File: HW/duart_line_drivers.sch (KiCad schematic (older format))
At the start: 2 parts

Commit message: Added ram, vias, rtc and ide connector. Managed to delete Pluto's CPLD schemas.
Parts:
- removed U?: SC26C92, symbol SC26C92
- removed U?: MAX238, symbol MAX238
- added C1, C2, C3, C4, C5: 1.0uF, symbol CP_Small
- added C6: 0.1uF, symbol C
- added J1: RS232a, symbol Conn_02x05_Odd_Even
- added J2: RS232b, symbol Conn_02x05_Odd_Even
- added U3: MAX238, symbol MAX238-RESCUE-saturn
- added U4: SC28L92PLCC44, symbol SC28L92PLCC44
- added X1: 3.6864 MHz, Oscillators:Oscillator_DIP-8, symbol CXO_DIP8
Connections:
- net labels added: A[0..18], A[0..3], CTSa, CTSb, D0, D1, D2, D3, D4, D5, D6, D7, D[0..7], GND, RES, RS232CTSa, RS232CTSb, RS232RTSa, RS232RTSb, RS232RxDa, RS232RxDb, RS232TxDa, RS232TxDb, RTSa, RTSb, VCC, ~IRQ, ~MRD, ~MWR
- wire segments 0 -> 96
- no-connect marks 0 -> 23

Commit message: Address, databus and control signals added to RAM and ROM
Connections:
- net ~DUARTSEL: now reaches U4.39 (~CEN)
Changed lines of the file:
@@
 Sheet 3 6
 Title "Saturn SBC"
-Date "2017-06-28"
-Rev "1.0"
+Date "2017-12-23"
+Rev "0.1"
 Comp "Linux Grotto"
 Comment1 ""
@@
 Wire Wire Line
 	2100 3650 2025 3650
+Text HLabel 7800 3625 2    60   Input ~ 0
+~DUARTSEL
+Wire Wire Line
+	7400 3625 7800 3625
 $EndSCHEMATC

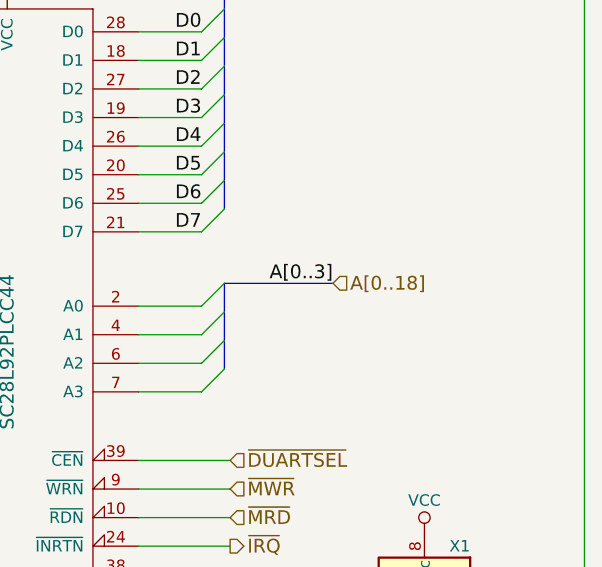
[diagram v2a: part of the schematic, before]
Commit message: Simulation of address decoding.
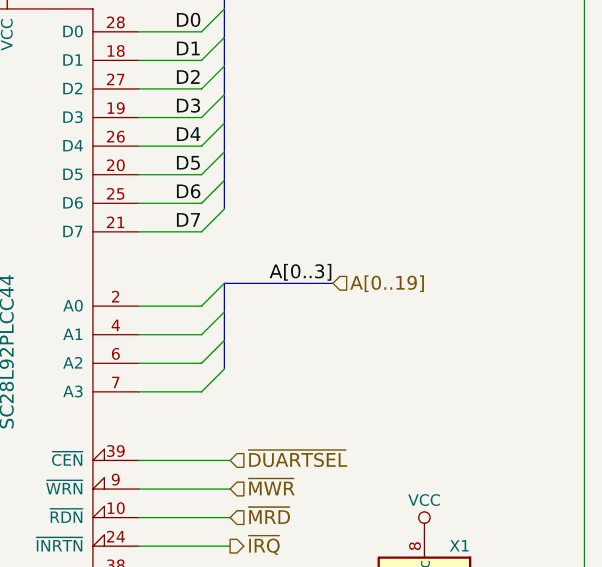
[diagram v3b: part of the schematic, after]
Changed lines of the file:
@@
 A[0..3]
 Text HLabel 8250 2850 2    60   Input ~ 0
-A[0..18]
+A[0..19]
 $Comp
 L MAX238-RESCUE-saturn U3
@@
 $EndComp
 $Comp
-L VCC #PWR5
+L VCC #PWR6
 U 1 1 5A14EA51
 P 4025 1225
-F 0 "#PWR5" H 4025 1075 50  0001 C CNN
+F 0 "#PWR6" H 4025 1075 50  0001 C CNN
 F 1 "VCC" H 4025 1375 50  0000 C CNN
 F 2 "" H 4025 1225 50  0001 C CNN
@@
 $EndComp
 $Comp
-L GND #PWR7
+L GND #PWR8
 U 1 1 5A14EB59
 P 5075 1350
-F 0 "#PWR7" H 5075 1100 50  0001 C CNN
+F 0 "#PWR8" H 5075 1100 50  0001 C CNN
 F 1 "GND" V 5075 1150 50  0000 C CNN
 F 2 "" H 5075 1350 50  0001 C CNN
@@
 $EndComp
 $Comp
-L GND #PWR4
+L GND #PWR5
 U 1 1 5A14F46D
 P 3125 2225
-F 0 "#PWR4" H 3125 1975 50  0001 C CNN
+F 0 "#PWR5" H 3125 1975 50  0001 C CNN
 F 1 "GND" H 3125 2075 50  0000 C CNN
 F 2 "" H 3125 2225 50  0001 C CNN
@@
 $EndComp
 $Comp
-L GND #PWR6
+L GND #PWR7
 U 1 1 5A14F656
 P 4025 4450
-F 0 "#PWR6" H 4025 4200 50  0001 C CNN
+F 0 "#PWR7" H 4025 4200 50  0001 C CNN
 F 1 "GND" H 4025 4300 50  0000 C CNN
 F 2 "" H 4025 4450 50  0001 C CNN
@@
 	1150 3550 1150 3725
 $Comp
-L GND #PWR3
+L GND #PWR4
 U 1 1 5A1536E4
 P 1150 3725
-F 0 "#PWR3" H 1150 3475 50  0001 C CNN
+F 0 "#PWR4" H 1150 3475 50  0001 C CNN
 F 1 "GND" H 1150 3575 50  0000 C CNN
 F 2 "" H 1150 3725 50  0001 C CNN
@@
 	1150 2825 1150 3000
 $Comp
-L GND #PWR2
+L GND #PWR3
 U 1 1 5A153732
 P 1150 3000
-F 0 "#PWR2" H 1150 2750 50  0001 C CNN
+F 0 "#PWR3" H 1150 2750 50  0001 C CNN
 F 1 "GND" H 1150 2850 50  0000 C CNN
 F 2 "" H 1150 3000 50  0001 C CNN
@@
 $EndComp
 $Comp
-L VCC #PWR10
+L VCC #PWR11
 U 1 1 5A1570C4
 P 8650 3950
-F 0 "#PWR10" H 8650 3800 50  0001 C CNN
+F 0 "#PWR11" H 8650 3800 50  0001 C CNN
 F 1 "VCC" H 8650 4100 50  0000 C CNN
 F 2 "" H 8650 3950 50  0001 C CNN
@@
 $EndComp
 $Comp
-L GND #PWR11
+L GND #PWR12
 U 1 1 5A157100
 P 8650 4550
-F 0 "#PWR11" H 8650 4300 50  0001 C CNN
+F 0 "#PWR12" H 8650 4300 50  0001 C CNN
 F 1 "GND" H 8650 4400 50  0000 C CNN
 F 2 "" H 8650 4550 50  0001 C CNN
@@
 	7400 4500 7800 4500
 $Comp
-L VCC #PWR9
+L VCC #PWR10
 U 1 1 5A157C4F
 P 7800 4500
-F 0 "#PWR9" H 7800 4350 50  0001 C CNN
+F 0 "#PWR10" H 7800 4350 50  0001 C CNN
 F 1 "VCC" V 7800 4675 50  0000 C CNN
 F 2 "" H 7800 4500 50  0001 C CNN
@@
 	6825 4900 6825 5325
 $Comp
-L GND #PWR8
+L GND #PWR9
 U 1 1 5A157EAF
 P 6825 5325
-F 0 "#PWR8" H 6825 5075 50  0001 C CNN
+F 0 "#PWR9" H 6825 5075 50  0001 C CNN
 F 1 "GND" H 6825 5175 50  0000 C CNN
 F 2 "" H 6825 5325 50  0001 C CNN

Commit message: ABEL code passes compilation, no tests though. Small changes to schema
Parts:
- added R5: 470, Resistors_ThroughHole:R_Axial_DIN0207_L6.3mm_D2.5mm_P2.54mm_Vertical, symbol R_Small
- C1, C2, C3, C4, C5: footprint (none) -> Capacitors_ThroughHole:CP_Radial_Tantal_D4.5mm_P2.50mm
- C6: footprint (none) -> Capacitors_ThroughHole:C_Disc_D4.7mm_W2.5mm_P5.00mm
- J1, J2: footprint (none) -> Connectors_IDC:IDC-Header_2x05_Pitch2.54mm_Straight
- U3: footprint (none) -> Housings_DIP:DIP-24_W7.62mm_Socket
- U4: footprint (none) -> saturn:PLCC-44_THT-Socket
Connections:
- net VCC: now also C6.2, U4.44 (VCC), R5.1
- net A0: now reaches U4.2 (A0)
- net at U4.36 (X1/CLK), X1.5 (OUT): now also R5.2
- net A1: now reaches U4.4 (A1)
- net A2: now reaches U4.6 (A2)
- net A3: now reaches U4.7 (A3)

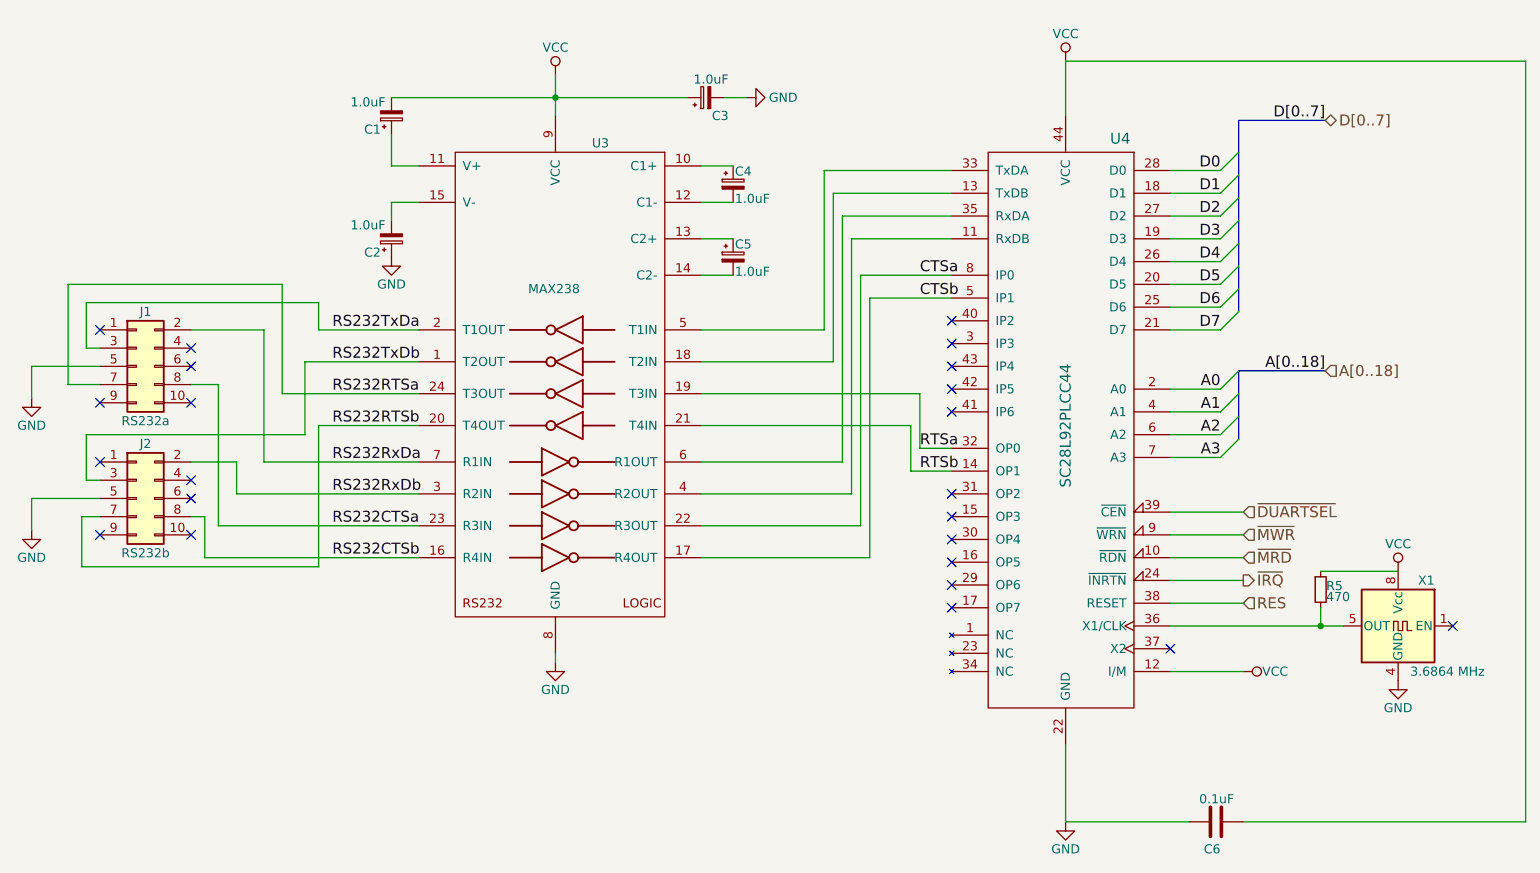
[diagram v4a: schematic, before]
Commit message: Added BDD CPLD code 0.5.1
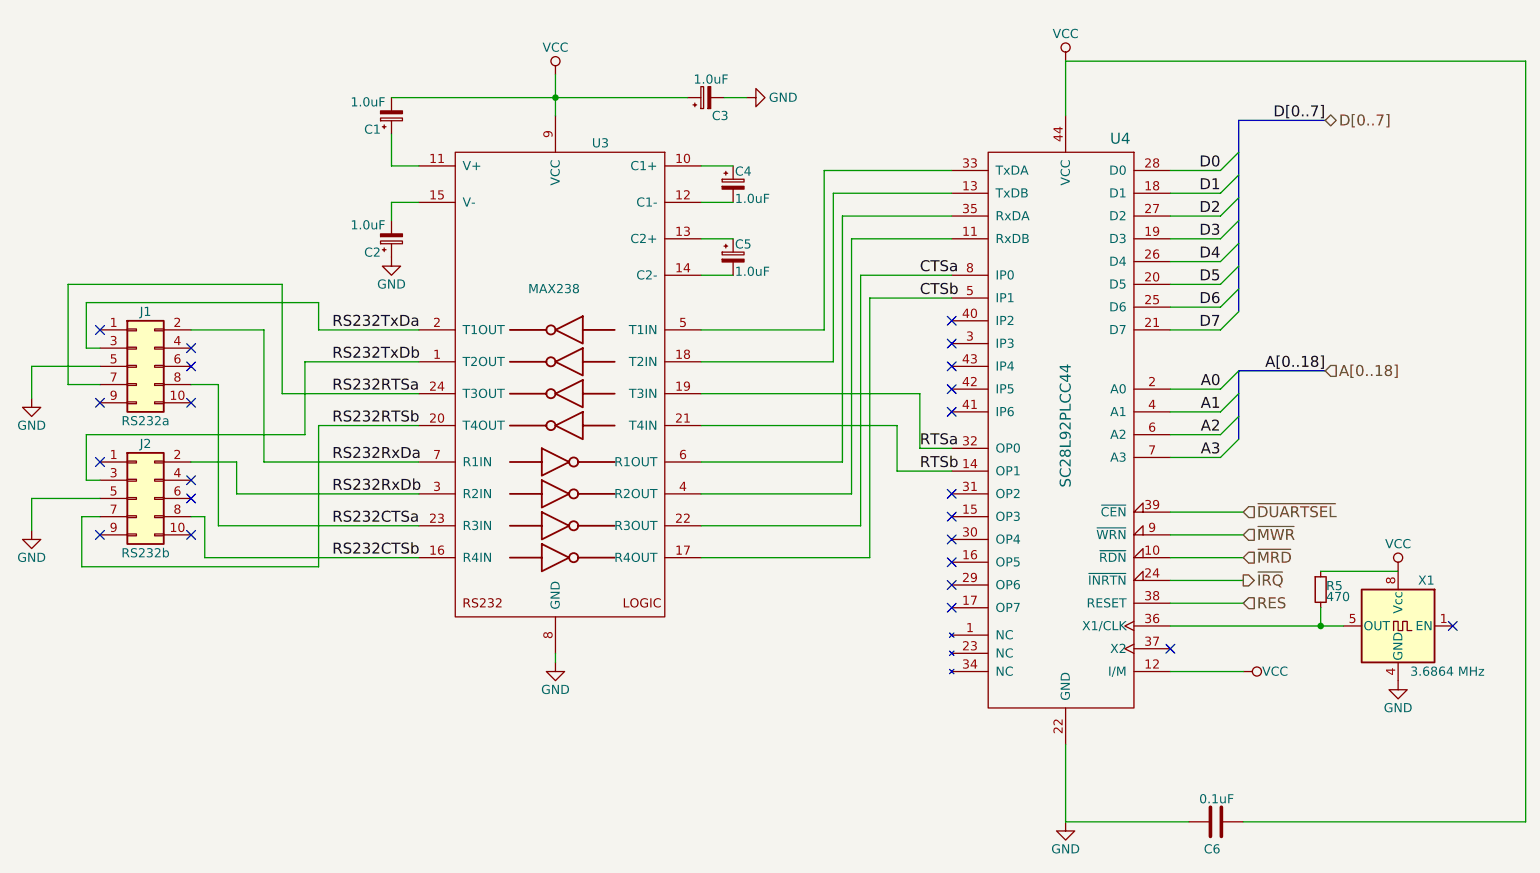
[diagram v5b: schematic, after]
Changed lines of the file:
@@
 	7400 2625 7675 2625
 Wire Bus Line
-	7775 1475 7775 2525
+	7775 1475 7775 1650
+Wire Bus Line
+	7775 1650 7775 1775
+Wire Bus Line
+	7775 1775 7775 1900
+Wire Bus Line
+	7775 1900 7775 2025
+Wire Bus Line
+	7775 2025 7775 2150
+Wire Bus Line
+	7775 2150 7775 2275
+Wire Bus Line
+	7775 2275 7775 2400
+Wire Bus Line
+	7775 2400 7775 2525
 Wire Bus Line
 	7775 1475 8250 1475
@@
 	7400 3325 7675 3325
 Wire Bus Line
-	7775 2850 7775 3225
+	7775 2850 7775 2975
+Wire Bus Line
+	7775 2975 7775 3100
+Wire Bus Line
+	7775 3100 7775 3225
 Wire Bus Line
 	7775 2850 8250 2850
@@
 	4825 2325 5000 2325
 Wire Wire Line
-	4025 1225 4025 1450
+	4025 1225 4025 1350
+Wire Wire Line
+	4025 1350 4025 1450
 Wire Wire Line
 	3275 1725 3125 1725
@@
 	3125 1725 3125 1550
 Wire Wire Line
-	3125 1350 4750 1350
+	3125 1350 4025 1350
+Wire Wire Line
+	4025 1350 4750 1350
 Connection ~ 4025 1350
 Wire Wire Line
@@
 	6200 3275 6025 3275
 Wire Wire Line
-	5975 3400 6200 3400
+	5900 3400 6200 3400
 Wire Wire Line
 	6200 1750 5500 1750
@@
 	6025 2975 4825 2975
 Wire Wire Line
-	5975 3400 5975 3150
+	5900 3400 5900 3150
 Wire Wire Line
-	5975 3150 4825 3150
+	5900 3150 4825 3150
 Wire Wire Line
 	5700 2325 5700 3700
@@
 	1425 3650 1525 3650
 Wire Wire Line
-	7400 4250 8350 4250
+	7400 4250 8225 4250
+Wire Wire Line
+	8225 4250 8350 4250
 Wire Wire Line
 	7400 4125 7800 4125

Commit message: Removed two ram chips, down to 1 MiB.
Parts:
- C1, C2, C3, C4, C5: symbol CP_Small -> device:CP_Small
- C6: symbol C -> device:C
- J1, J2: footprint Connectors_IDC:IDC-Header_2x05_Pitch2.54mm_Straight -> Connectors_IDC:IDC-Header_2x05_Pitch2.54mm_Angled; symbol Conn_02x05_Odd_Even -> saturn-rescue:Conn_02x05_Odd_Even
- R5: symbol R_Small -> device:R_Small
- U3: symbol MAX238-RESCUE-saturn -> saturn-rescue:MAX238-RESCUE-saturn
- U4: symbol SC28L92PLCC44 -> saturn:SC28L92PLCC44
- X1: symbol CXO_DIP8 -> Oscillators:CXO_DIP8
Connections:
- no-connect marks 23 -> 24
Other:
- note added: "DUART (00:FEE0 - 00:FEEF)"
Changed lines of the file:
@@
-EESchema Schematic File Version 2
-LIBS:saturn-rescue
-LIBS:power
-LIBS:device
-LIBS:transistors
-LIBS:conn
-LIBS:linear
-LIBS:regul
-LIBS:74xx
-LIBS:cmos4000
-LIBS:adc-dac
-LIBS:memory
-LIBS:xilinx
-LIBS:microcontrollers
-LIBS:dsp
-LIBS:microchip
-LIBS:analog_switches
-LIBS:motorola
-LIBS:texas
-LIBS:intel
-LIBS:audio
-LIBS:interface
-LIBS:digital-audio
-LIBS:philips
-LIBS:display
-LIBS:cypress
-LIBS:siliconi
-LIBS:opto
-LIBS:atmel
-LIBS:contrib
-LIBS:valves
-LIBS:saturn
-LIBS:65xx
-LIBS:pluto
-LIBS:Oscillators
-LIBS:switches
+EESchema Schematic File Version 4
 LIBS:saturn-cache
-EELAYER 25 0
+EELAYER 26 0
 EELAYER END
 $Descr A4 11693 8268
 encoding utf-8
-Sheet 3 7
+Sheet 3 6
 Title "DUART SC28L92 and line driver"
 Date "2018-01-17"
@@
 A[0..18]
 $Comp
-L MAX238-RESCUE-saturn U3
+L saturn-rescue:MAX238-RESCUE-saturn U3
 U 1 1 5A14E417
 P 4025 3050
@@
 $EndComp
 $Comp
-L CP_Small C4
+L device:CP_Small C4
 U 1 1 5A14E4E1
 P 5000 1825
@@
 $EndComp
 $Comp
-L CP_Small C5
+L device:CP_Small C5
 U 1 1 5A14E779
 P 5000 2225
@@
 $EndComp
 $Comp
-L CP_Small C1
+L device:CP_Small C1
 U 1 1 5A14E8FA
 P 3125 1450
@@
 $EndComp
 $Comp
-L VCC #PWR017
+L power1:VCC #PWR025
 U 1 1 5A14EA51
 P 4025 1225
-F 0 "#PWR017" H 4025 1075 50  0001 C CNN
+F 0 "#PWR025" H 4025 1075 50  0001 C CNN
 F 1 "VCC" H 4025 1375 50  0000 C CNN
 F 2 "" H 4025 1225 50  0001 C CNN
@@
 $EndComp
 $Comp
-L CP_Small C3
+L device:CP_Small C3
 U 1 1 5A14EA93
 P 4850 1350
@@
 $EndComp
 $Comp
-L GND #PWR018
+L power1:GND #PWR026
 U 1 1 5A14EB59
 P 5075 1350
-F 0 "#PWR018" H 5075 1100 50  0001 C CNN
+F 0 "#PWR026" H 5075 1100 50  0001 C CNN
 F 1 "GND" V 5075 1150 50  0000 C CNN
 F 2 "" H 5075 1350 50  0001 C CNN
@@
 $EndComp
 $Comp
-L CP_Small C2
+L device:CP_Small C2
 U 1 1 5A14F3DD
 P 3125 2125
@@
 $EndComp
 $Comp
-L GND #PWR019
+L power1:GND #PWR027
 U 1 1 5A14F46D
 P 3125 2225
-F 0 "#PWR019" H 3125 1975 50  0001 C CNN
+F 0 "#PWR027" H 3125 1975 50  0001 C CNN
 F 1 "GND" H 3125 2075 50  0000 C CNN
 F 2 "" H 3125 2225 50  0001 C CNN
@@
 $EndComp
 $Comp
-L GND #PWR020
+L power1:GND #PWR028
 U 1 1 5A14F656
 P 4025 4450
-F 0 "#PWR020" H 4025 4200 50  0001 C CNN
+F 0 "#PWR028" H 4025 4200 50  0001 C CNN
 F 1 "GND" H 4025 4300 50  0000 C CNN
 F 2 "" H 4025 4450 50  0001 C CNN
@@
 $EndComp
 $Comp
-L SC28L92PLCC44 U4
+L saturn:SC28L92PLCC44 U4
 U 1 1 5A14F76D
 P 6725 2600
@@
 RTSb
 $Comp
-L Conn_02x05_Odd_Even J1
+L saturn-rescue:Conn_02x05_Odd_Even J1
 U 1 1 5A152192
 P 1725 2825
+AR Path="/5A152192" Ref="J1"  Part="1"
+AR Path="/5952FC81/5A152192" Ref="J1"  Part="1"
 F 0 "J1" H 1775 3125 50  0000 C CNN
 F 1 "RS232a" H 1775 2525 50  0000 C CNN
-F 2 "Connectors_IDC:IDC-Header_2x05_Pitch2.54mm_Straight" H 1725 2825 50  0001 C CNN
+F 2 "Connectors_IDC:IDC-Header_2x05_Pitch2.54mm_Angled" H 1725 2825 50  0001 C CNN
 F 3 "" H 1725 2825 50  0001 C CNN
 	1    1725 2825
@@
 $EndComp
 $Comp
-L Conn_02x05_Odd_Even J2
+L saturn-rescue:Conn_02x05_Odd_Even J2
 U 1 1 5A15222D
 P 1725 3550
+AR Path="/5A15222D" Ref="J2"  Part="1"
+AR Path="/5952FC81/5A15222D" Ref="J2"  Part="1"
 F 0 "J2" H 1775 3850 50  0000 C CNN
 F 1 "RS232b" H 1775 3250 50  0000 C CNN
-F 2 "Connectors_IDC:IDC-Header_2x05_Pitch2.54mm_Straight" H 1725 3550 50  0001 C CNN
+F 2 "Connectors_IDC:IDC-Header_2x05_Pitch2.54mm_Angled" H 1725 3550 50  0001 C CNN
 F 3 "" H 1725 3550 50  0001 C CNN
 	1    1725 3550
@@
 RS232CTSb
 $Comp
-L GND #PWR021
+L power1:GND #PWR029
 U 1 1 5A1536E4
 P 1150 3725
-F 0 "#PWR021" H 1150 3475 50  0001 C CNN
+F 0 "#PWR029" H 1150 3475 50  0001 C CNN
 F 1 "GND" H 1150 3575 50  0000 C CNN
 F 2 "" H 1150 3725 50  0001 C CNN
@@
 $EndComp
 $Comp
-L GND #PWR022
+L power1:GND #PWR030
 U 1 1 5A153732
 P 1150 3000
-F 0 "#PWR022" H 1150 2750 50  0001 C CNN
+F 0 "#PWR030" H 1150 2750 50  0001 C CNN
 F 1 "GND" H 1150 2850 50  0000 C CNN
 F 2 "" H 1150 3000 50  0001 C CNN
@@
 NoConn ~ 6200 4150
 $Comp
-L CXO_DIP8 X1
+L Oscillators:CXO_DIP8 X1
 U 1 1 5A156C53
 P 8650 4250
@@
 $EndComp
 $Comp
-L VCC #PWR023
+L power1:VCC #PWR031
 U 1 1 5A1570C4
 P 8650 3950
-F 0 "#PWR023" H 8650 3800 50  0001 C CNN
+F 0 "#PWR031" H 8650 3800 50  0001 C CNN
 F 1 "VCC" H 8650 4100 50  0000 C CNN
 F 2 "" H 8650 3950 50  0001 C CNN
@@
 $EndComp
 $Comp
-L GND #PWR024
+L power1:GND #PWR032
 U 1 1 5A157100
 P 8650 4550
-F 0 "#PWR024" H 8650 4300 50  0001 C CNN
+F 0 "#PWR032" H 8650 4300 50  0001 C CNN
 F 1 "GND" H 8650 4400 50  0000 C CNN
 F 2 "" H 8650 4550 50  0001 C CNN
@@
 NoConn ~ 7400 4375
 $Comp
-L VCC #PWR025
+L power1:VCC #PWR033
 U 1 1 5A157C4F
 P 7800 4500
-F 0 "#PWR025" H 7800 4350 50  0001 C CNN
+F 0 "#PWR033" H 7800 4350 50  0001 C CNN
 F 1 "VCC" V 7800 4675 50  0000 C CNN
 F 2 "" H 7800 4500 50  0001 C CNN
@@
 $EndComp
 $Comp
-L GND #PWR026
+L power1:GND #PWR034
 U 1 1 5A157EAF
 P 6825 5325
-F 0 "#PWR026" H 6825 5075 50  0001 C CNN
+F 0 "#PWR034" H 6825 5075 50  0001 C CNN
 F 1 "GND" H 6825 5175 50  0000 C CNN
 F 2 "" H 6825 5325 50  0001 C CNN
@@
 $EndComp
 $Comp
-L C C6
+L device:C C6
 U 1 1 5A157F44
 P 7650 5325
@@
 ~DUARTSEL
 $Comp
-L R_Small R5
+L device:R_Small R5
 U 1 1 5A984B90
 P 8225 4050
@@
 	7400 2625 7675 2625
 Wire Bus Line
-	7775 1475 7775 1650
-Wire Bus Line
-	7775 1650 7775 1775
-Wire Bus Line
-	7775 1775 7775 1900
-Wire Bus Line
-	7775 1900 7775 2025
-Wire Bus Line
-	7775 2025 7775 2150
-Wire Bus Line
-	7775 2150 7775 2275
-Wire Bus Line
-	7775 2275 7775 2400
-Wire Bus Line
-	7775 2400 7775 2525
-Wire Bus Line
 	7775 1475 8250 1475
 Wire Wire Line
@@
 	7400 3325 7675 3325
 Wire Bus Line
-	7775 2850 7775 2975
-Wire Bus Line
-	7775 2975 7775 3100
-Wire Bus Line
-	7775 3100 7775 3225
-Wire Bus Line
 	7775 2850 8250 2850
 Wire Wire Line
@@
 	4025 1225 4025 1350
 Wire Wire Line
-	4025 1350 4025 1450
-Wire Wire Line
 	3275 1725 3125 1725
 Wire Wire Line
@@
 Wire Wire Line
 	3125 1350 4025 1350
-Wire Wire Line
-	4025 1350 4750 1350
 Connection ~ 4025 1350
 Wire Wire Line
@@
 Wire Wire Line
 	7400 4250 8225 4250
-Wire Wire Line
-	8225 4250 8350 4250
 Wire Wire Line
 	7400 4125 7800 4125
@@
 A3
 $Comp
-L VCC #PWR027
+L power1:VCC #PWR035
 U 1 1 5AA1B80C
 P 6825 1150
-F 0 "#PWR027" H 6825 1000 50  0001 C CNN
+F 0 "#PWR035" H 6825 1000 50  0001 C CNN
 F 1 "VCC" H 6825 1300 50  0000 C CNN
 F 2 "" H 6825 1150 50  0001 C CNN
@@
 	1    0    0    -1
 $EndComp
+Wire Wire Line
+	4025 1350 4025 1450
+Wire Wire Line
+	4025 1350 4750 1350
+Wire Wire Line
+	8225 4250 8350 4250
+NoConn ~ 4575 3850
+Wire Bus Line
+	7775 2850 7775 3225
+Wire Bus Line
+	7775 1475 7775 2525
+Text Notes 7200 1000 0    60   ~ 12
+DUART (00:FEE0 - 00:FEEF)
 $EndSCHEMATC
